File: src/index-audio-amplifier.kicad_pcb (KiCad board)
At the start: 2 copper layers, 23.5 x 23.5 mm, 61 parts, among them J1 CU3616SASCLA004-LF, J2 SWD_PicoprobeCandybar, J3 Conn_01x02, J4 Conn_01x02, U1 RP2040, U2 RT6150B-33GQW, U3 W25Q16JVUXIQ, U4 MAX98360CENL, U5 TLV70033_SOT23-5, U6 MAX98360CENL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

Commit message: Continue refactoring very compact layout
Feeling pretty good about this second attempt so far...
Next up: analogue and power regulation
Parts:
- C14, R10, R12, R13, R2: moved to F.Cu
- C15, C18, C23, C24, C25, C26, R15, R17, R6, R7, R9, U3, X2: moved to B.Cu
- moved C13 64.9 mm to (151.0, 104.1), turned to 90 degrees
- moved C6 64.7 mm to (152.5, 106.7), turned to 0 degrees
- moved C5 64.3 mm to (152.5, 107.7), turned to 0 degrees
- moved C4 64.0 mm to (152.5, 108.7), turned to 0 degrees
- moved C7 63.3 mm to (152.5, 105.8), turned to 0 degrees
- moved C8 62.1 mm to (152.5, 104.9), turned to 0 degrees
- moved C10 60.8 mm to (152.5, 103.9), turned to 0 degrees
- moved C14 57.3 mm to (158.0, 99.6), turned to 90 degrees
- moved C16 56.4 mm to (157.5, 109.1)
- moved X1 53.8 mm to (158.0, 106.0), turned to 90 degrees
- moved C17 52.4 mm to (158.5, 109.1), turned to -90 degrees
- moved R14 50.9 mm to (158.6, 103.3)
- moved R7 49.1 mm to (138.3, 106.4)
- moved R9 48.8 mm to (138.3, 105.5), turned to 180 degrees
- moved R6 44.6 mm to (142.5, 98.3), turned to -90 degrees
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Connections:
- net Net-(U1-GPIO25) renamed /LED
- U1 pad 2: unconnected-(U1-GPIO0-Pad2) -> /HUB_SMDT
- U1 pad 3: unconnected-(U1-GPIO1-Pad3) -> /HUB_SMCK
- U1 pad 38: /HUB_SUSP -> unconnected-(U1-GPIO26_ADC0-Pad38)
- U1 pad 39: /HUB_RST -> unconnected-(U1-GPIO27_ADC1-Pad39)
- U1 pad 4: unconnected-(U1-GPIO2-Pad4) -> /HUB_RST
- U1 pad 40: /HUB_SMCK -> unconnected-(U1-GPIO28_ADC2-Pad40)
- U1 pad 41: /HUB_SMDT -> unconnected-(U1-GPIO29_ADC3-Pad41)
- U1 pad 5: unconnected-(U1-GPIO3-Pad5) -> /HUB_SUSP
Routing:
- net /AUX_DM: track 8.19 -> 27.4 mm
- net /AUX_DP: track 8.05 -> 25.5 mm
- net +3V3: track 0.60 -> 16.2 mm, vias 0 -> 6
- net /HUB_SMDT: track 0.00 -> 15.5 mm, vias 0 -> 2
- net /HUB_SMCK: track 0.00 -> 14.2 mm, vias 0 -> 2
- net /HUB_SUSP: track 0.00 -> 13.4 mm, vias 0 -> 2
- net Net-(J1B-CC1_UP): track 0.00 -> 12.0 mm
- net /HUB_RST: track 0.00 -> 11.3 mm, vias 0 -> 2
- net Net-(J2-SWDIO): track 0.00 -> 10.2 mm
- net Net-(J1B-CC2_UP): track 0.00 -> 10.1 mm
- net Net-(U7-VBUS_DET): track 0.00 -> 8.16 mm, vias 0 -> 1
- net /DP_IN: track 9.28 -> 17.3 mm
- net Net-(U7-XTALIN): track 0.00 -> 7.46 mm, vias 0 -> 1
- net /DM_IN: track 11.6 -> 19.0 mm
- net VSYS: track 7.44 -> 14.4 mm
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- added copper zone on F.Cu, net VBUS

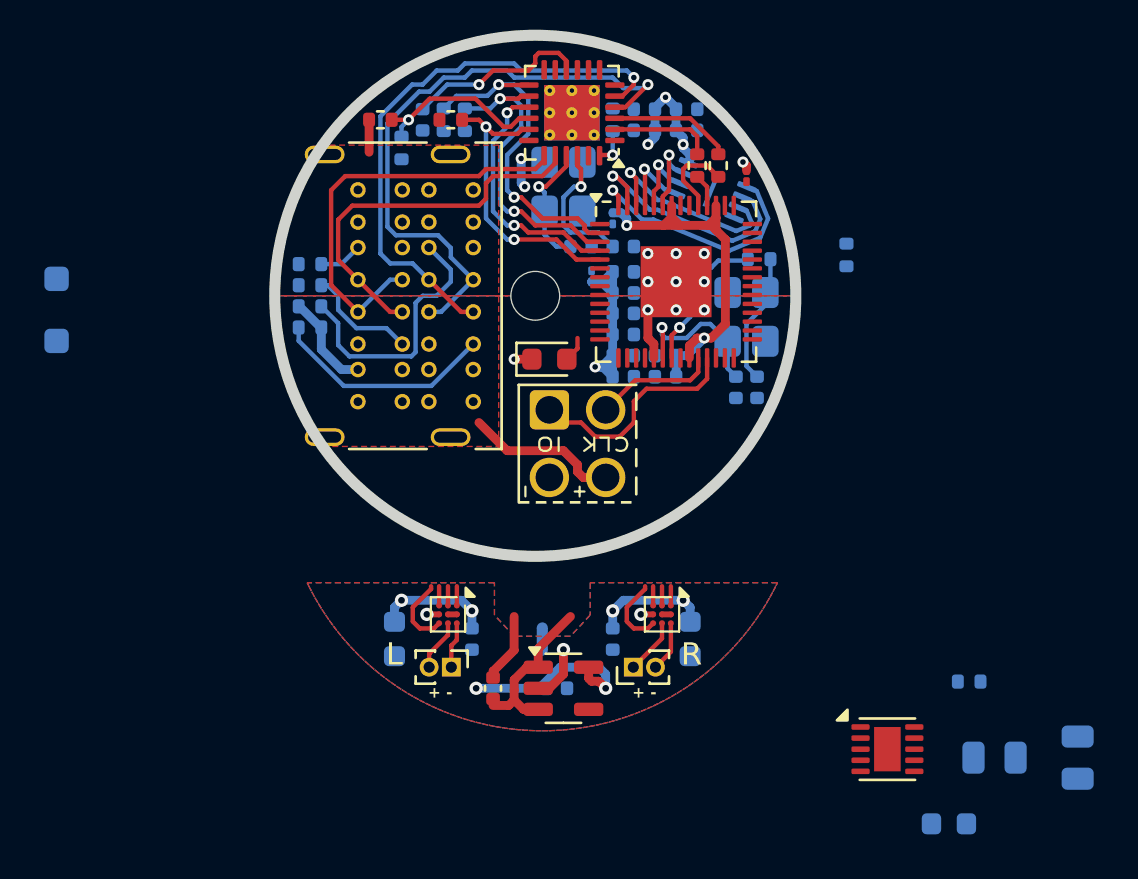
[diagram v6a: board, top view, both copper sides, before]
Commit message: Complete initial PCB layout :)
Remaining DRC errors/warnings should seemingly be "fine"

The analogue layout (arguably the most important part) was very cramped
at the end.  If refactoring, consider prioritizing analogue as well as
decoupling capacitor layout first next time.

But - feels good to have condensed everything into this tiny footprint!!
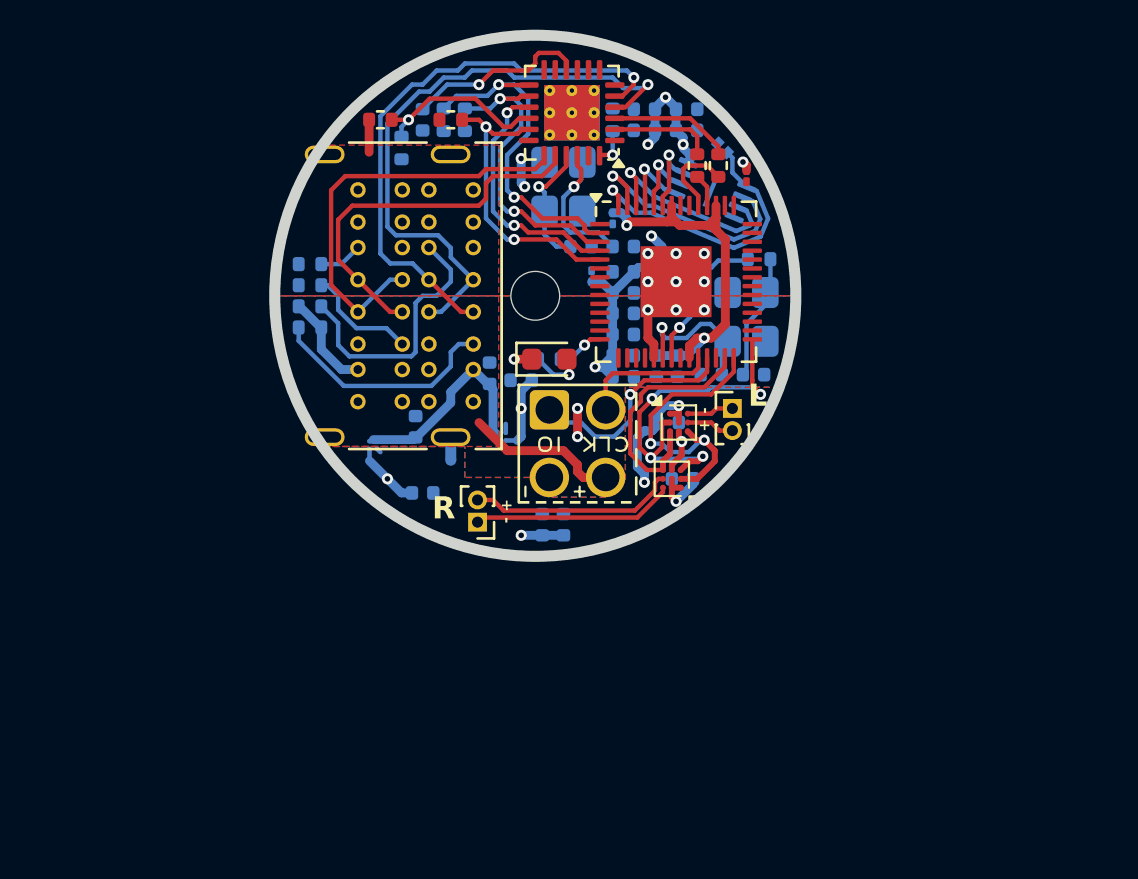
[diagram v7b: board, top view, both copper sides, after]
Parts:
- removed D1: MBR120VLSFT1G, Diode_SMD:D_SOD-123F
- removed L1: 2u2, Inductor_SMD:L_0603_1608Metric
- removed R8: 100K, Resistor_SMD:R_0402_1005Metric
- added JP1: 3V3_EN, ProjectFootprints_IndexAudioAmplifier:SolderJumper-2_P1.0mm_Open_RoundedPad0.5x1.0mm, B.Cu at (156.9, 98.3)
- C1, C2: value 47u -> 1u; footprint Capacitor_SMD:C_0805_2012Metric -> Capacitor_SMD:C_0402_1005Metric
- C101: moved to B.Cu
- C19, C21: footprint Capacitor_SMD:C_0603_1608Metric -> Capacitor_SMD:C_0402_1005Metric
- D2: value Green -> Blue
- U2: value RT6150B-33GQW -> NCP167; footprint Package_SON:WSON-10-1EP_2.5x2.5mm_P0.5mm_EP1.2x2mm -> Package_CSP:WLCSP-4_0.64x0.64mm_Layout2x2_P0.35mm; moved to B.Cu
- U5: value TLV70033_SOT23-5 -> NCP167; footprint Package_TO_SOT_SMD:SOT-23-5 -> Package_CSP:WLCSP-4_0.64x0.64mm_Layout2x2_P0.35mm; moved to B.Cu
- moved C2 30.3 mm to (147.9, 108.8), turned to 180 degrees
- moved C1 28.6 mm to (146.4, 108.5), turned to 90 degrees
- moved U2 22.4 mm to (147.0, 111.3)
- moved J4 17.2 mm to (157.4, 110.1), turned to 0 degrees
- moved C21 14.9 mm to (155.1, 113.3), turned to 180 degrees
- moved R3 14.2 mm to (149.1, 107.9), turned to 180 degrees
- moved U5 13.9 mm to (141.2, 111.7), turned to -90 degrees
- moved U4 13.5 mm to (155.0, 110.7), turned to 0 degrees
- moved C101 12.3 mm to (143.1, 110.9)
- moved C102 10.7 mm to (143.4, 113.9)
- moved C20 10.1 mm to (154.5, 110.7), turned to 0 degrees
- moved J3 9.60 mm to (145.9, 115.2), turned to 180 degrees
- moved NT1 9.51 mm to (144.7, 111.9)
- moved C19 8.43 mm to (148.8, 115.3), turned to 90 degrees
- moved C22 6.60 mm to (149.8, 115.3), turned to 90 degrees
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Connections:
- C1 pad 1: VSYS -> VBUS
- C101 pad 1: VSYS -> VBUS
- J2 pad 4: VSYS -> VBUS
- J3 pad 1: /RIGHT_P -> /RIGHT_N
- J3 pad 2: /RIGHT_N -> /RIGHT_P
- U1 pad 14: unconnected-(U1-GPIO11-Pad14) -> /LED
- U1 pad 18: /AMP_EN -> unconnected-(U1-GPIO15-Pad18)
- U1 pad 30: unconnected-(U1-GPIO19-Pad30) -> /AMP_EN
- U1 pad 35: /GPIO23 -> unconnected-(U1-GPIO23-Pad35)
- U1 pad 37: /LED -> unconnected-(U1-GPIO25-Pad37)
- U4 pad A1: /AMP_EN -> +3V3A
- U6 pad A1: /AMP_EN -> +3V3A
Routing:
- net VBUS: track 5.89 -> 23.4 mm
- net /AMP_DATA: track 1.74 -> 16.9 mm, vias 0 -> 4
- net VSYS: track 14.4 -> 0.00 mm
- net /AMP_FCLK: track 4.22 -> 13.2 mm, vias 0 -> 2
- net /AMP_BCLK: track 4.22 -> 11.2 mm
- net /RIGHT_N: track 2.27 -> 9.05 mm
- net /RIGHT_P: track 2.52 -> 9.30 mm
- net +3V3A: track 19.8 -> 13.9 mm, vias 6 -> 5
- net +3V3: track 16.2 -> 21.6 mm, vias 6 -> 8
- net /LED: track 0.00 -> 2.14 mm, vias 0 -> 1
- net Net-(JP1-A): track 11.2 -> 12.9 mm
- net /AMP_EN: track 1.74 -> 0.00 mm
- net AGND: track 3.62 -> 2.18 mm, vias 3 -> 1
- net Net-(D2-A): track 1.15 -> 2.43 mm, vias 0 -> 1
- net GND: track 10.1 -> 8.90 mm, vias 11 -> 13
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
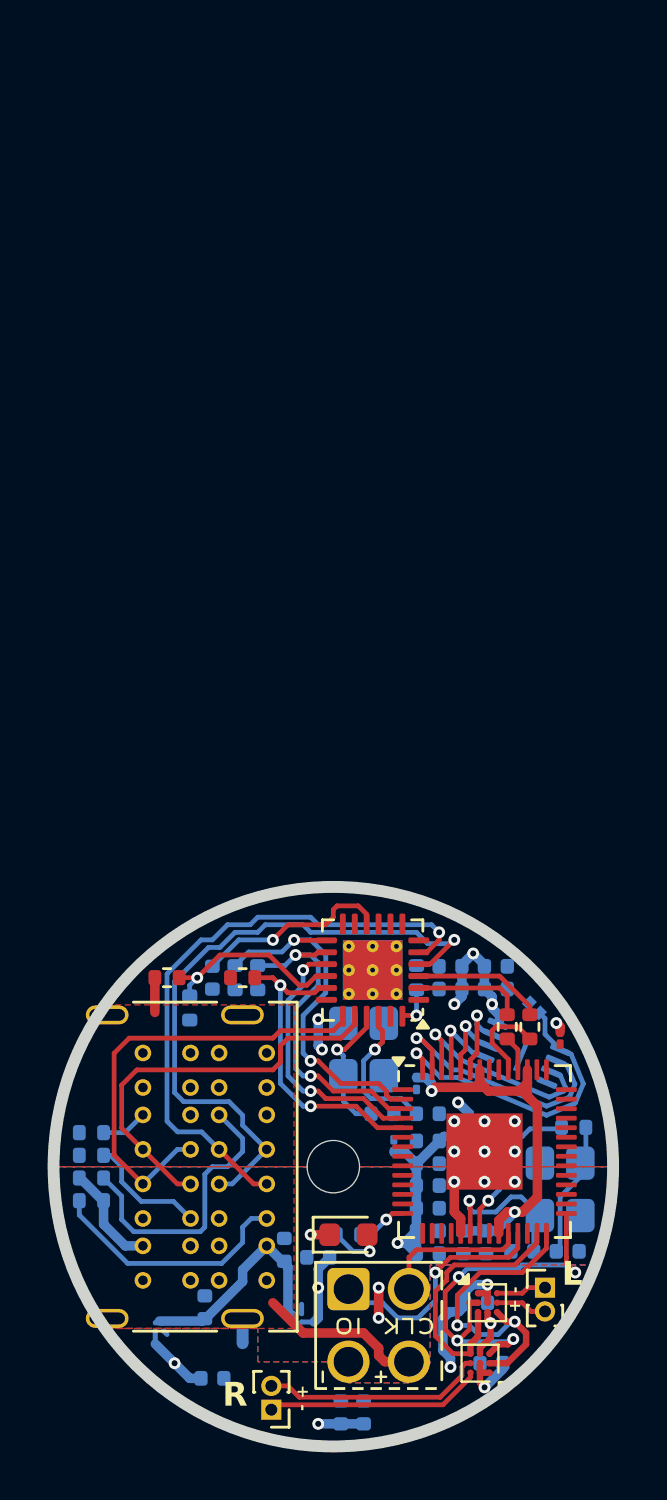
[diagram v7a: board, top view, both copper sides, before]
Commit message: Reposition origin & rotate Index reference drawing
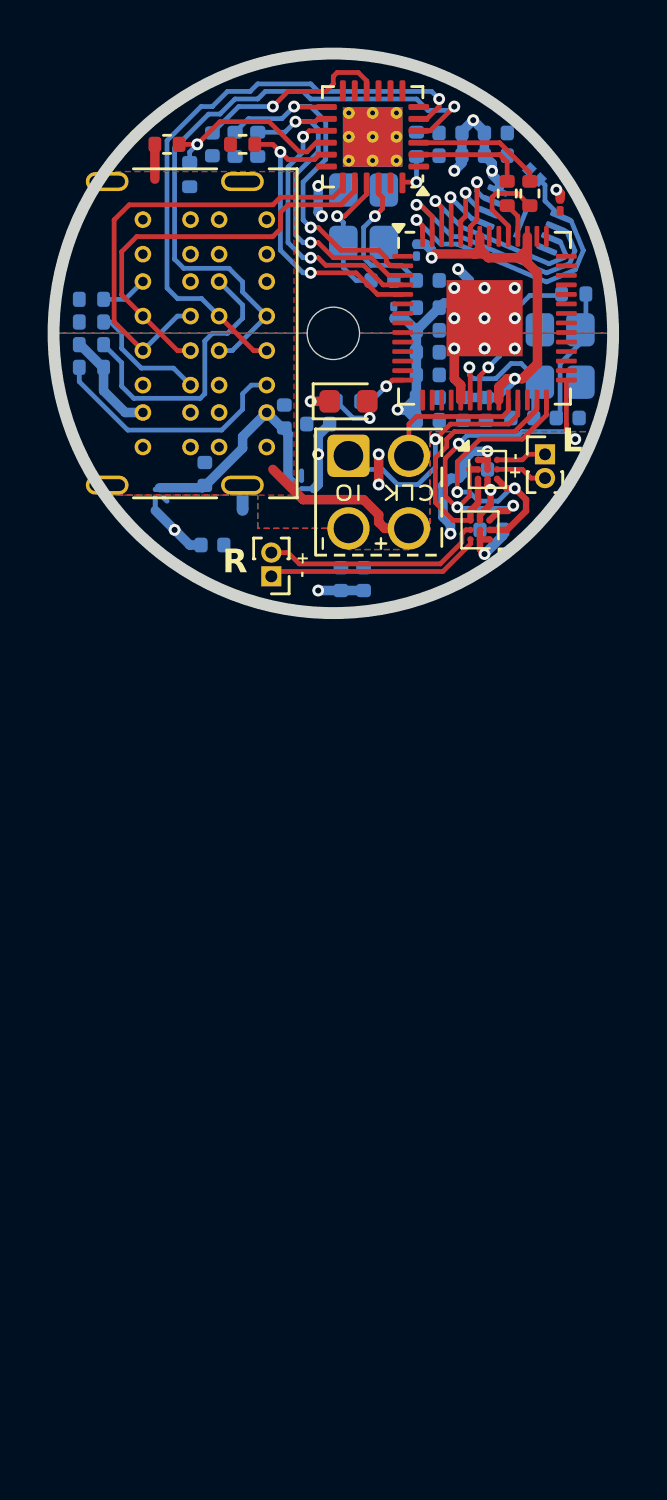
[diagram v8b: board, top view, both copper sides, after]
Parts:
- JP1: value 3V3_EN -> BOOTSEL
- moved C15 35.0 mm to (155.3, 61.6)
- moved C24 35.0 mm to (153.4, 61.6)
- moved U7 35.0 mm to (150.2, 61.7)
- moved C1 35.0 mm to (146.4, 73.5)
- moved C10 35.0 mm to (152.5, 68.9)
- moved C101 35.0 mm to (143.1, 75.9)
- moved C102 35.0 mm to (143.4, 78.9)
- moved C11 35.0 mm to (154.9, 73.2)
- moved C12 35.0 mm to (152.0, 66.5)
- moved C13 35.0 mm to (151.0, 69.1)
- moved C14 35.0 mm to (158.0, 64.6)
- moved C16 35.0 mm to (156.4, 73.6)
- moved C17 35.0 mm to (158.3, 73.6)
- moved C19 35.0 mm to (148.8, 80.3)
- moved C2 35.0 mm to (147.9, 73.8)
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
